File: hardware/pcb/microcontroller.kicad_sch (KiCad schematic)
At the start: 16 parts, among them U4 STM32G474CBT6TR, Y1 CS10820-24M

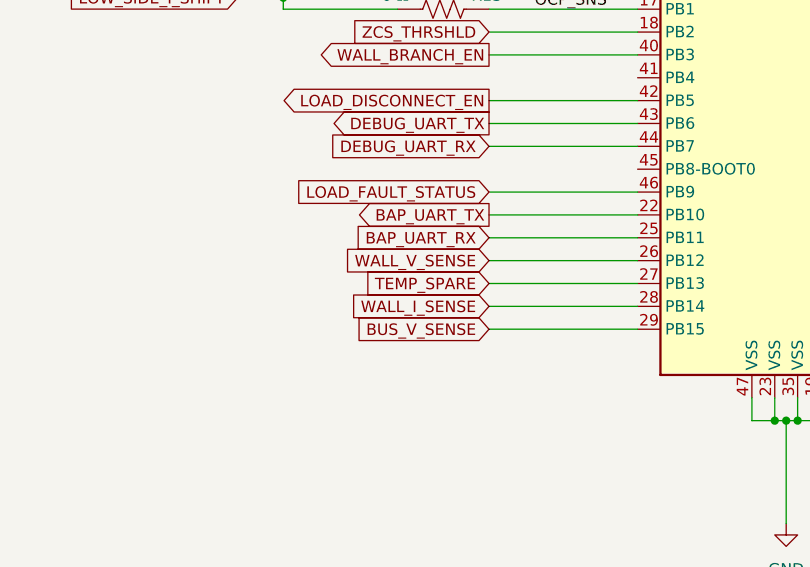
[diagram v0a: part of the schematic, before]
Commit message: Assign PB13 to delivered-load voltage sensing
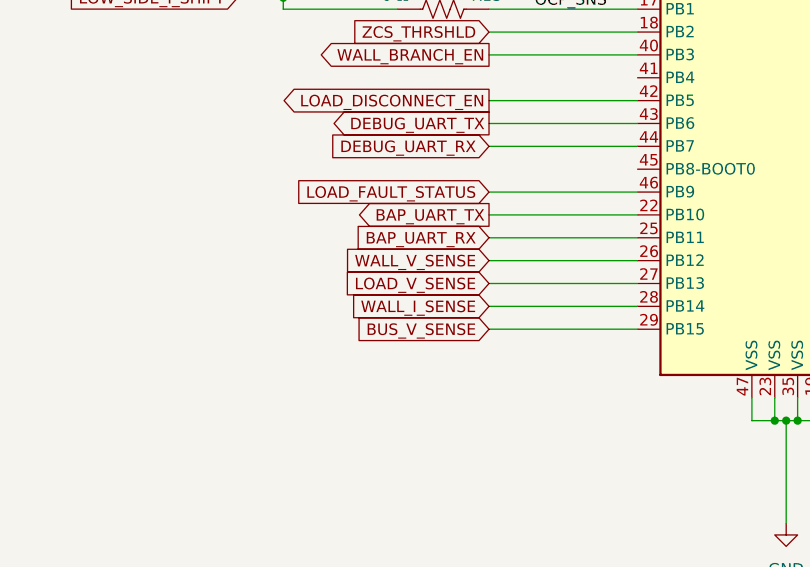
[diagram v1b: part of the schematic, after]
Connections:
- net TEMP_SPARE renamed LOAD_V_SENSE
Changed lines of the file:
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@@
 		)
 	)
-	(global_label "TEMP_SPARE"
+	(global_label "LOAD_V_SENSE"
 		(shape input)
 		(at 121.92 139.7 180)

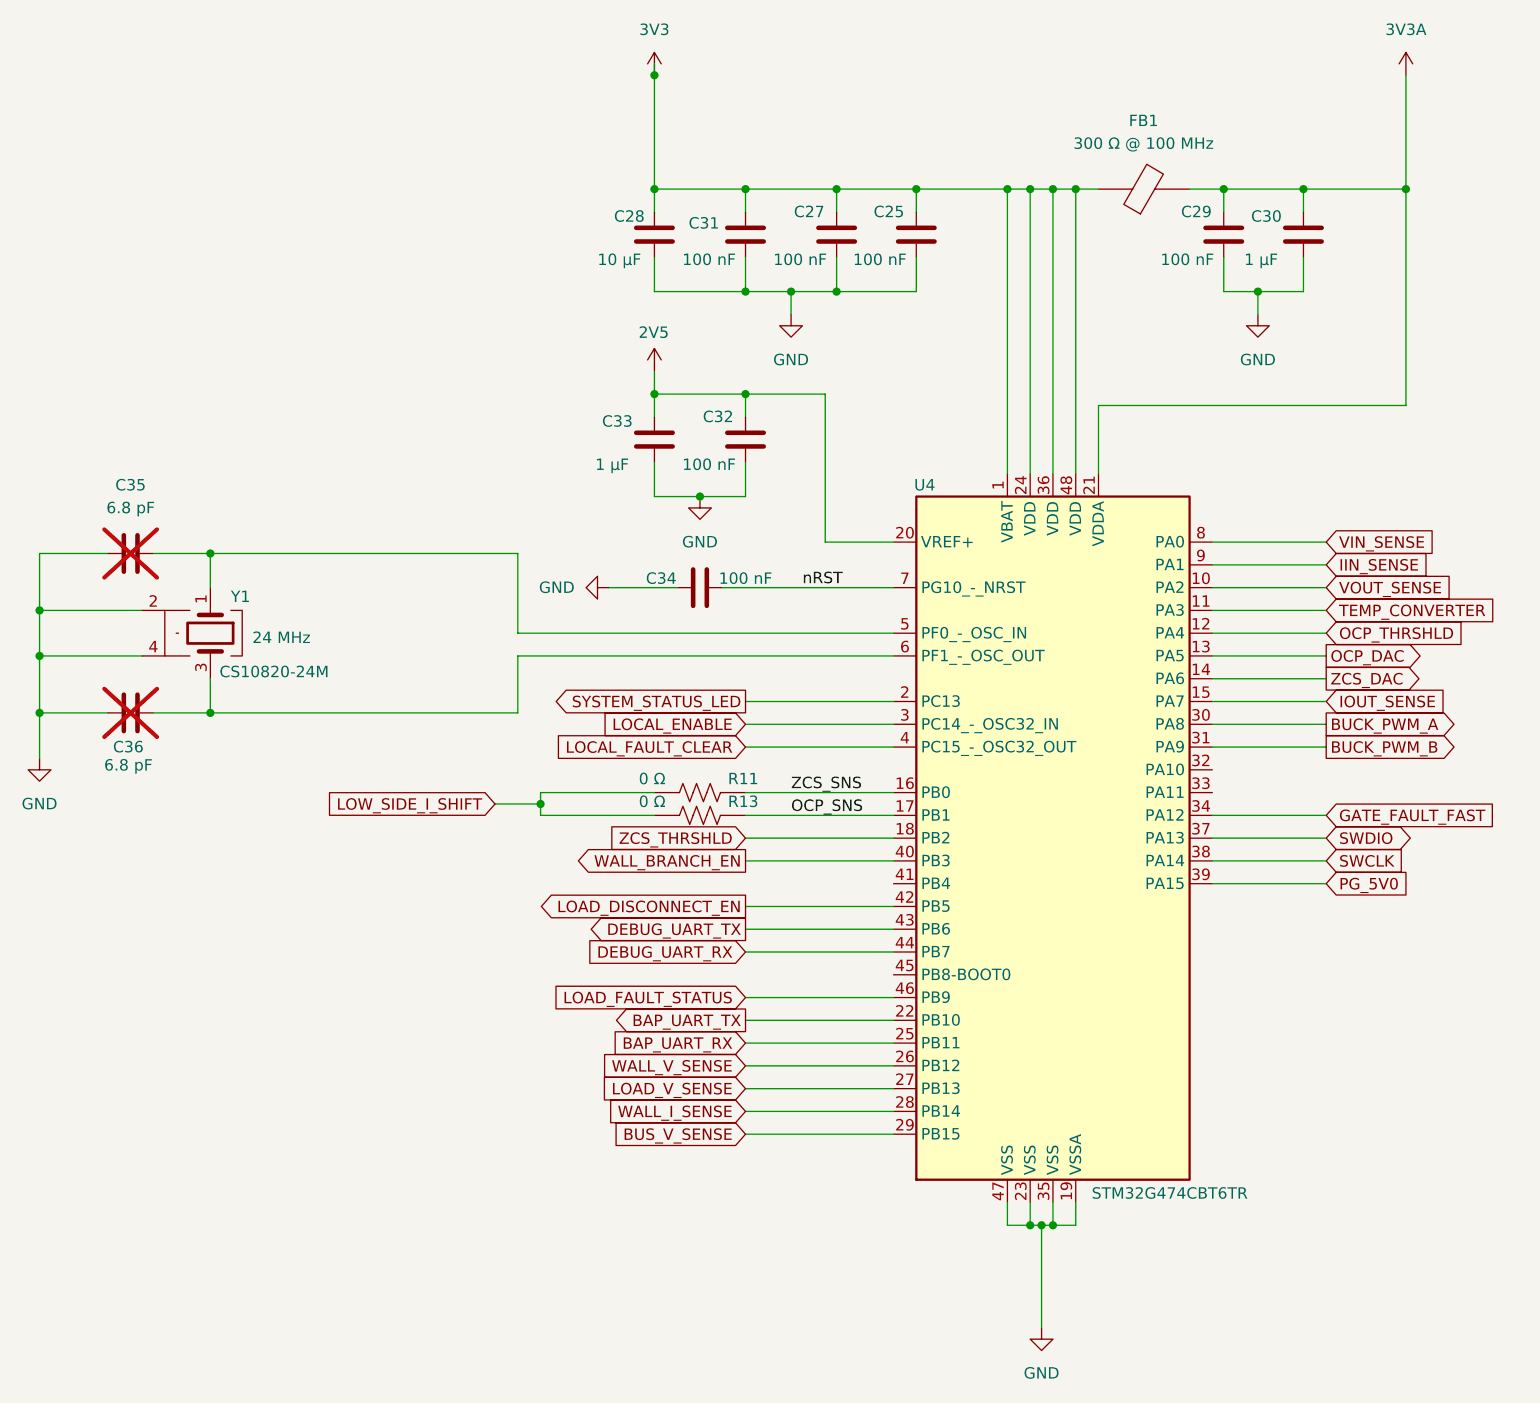
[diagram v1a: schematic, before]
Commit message: Replace legacy passive Specs with verified exact-MPN components
Migrate 51 instances across 20 identities and advance the public library pin to 8a4c96de. Preserve component references, UUIDs, placement, DNP flags, shared package geometry/models and exact pin-to-net connectivity. All ERC findings match baseline; PCB and unrelated components unchanged. Includes per-reference replacement report.
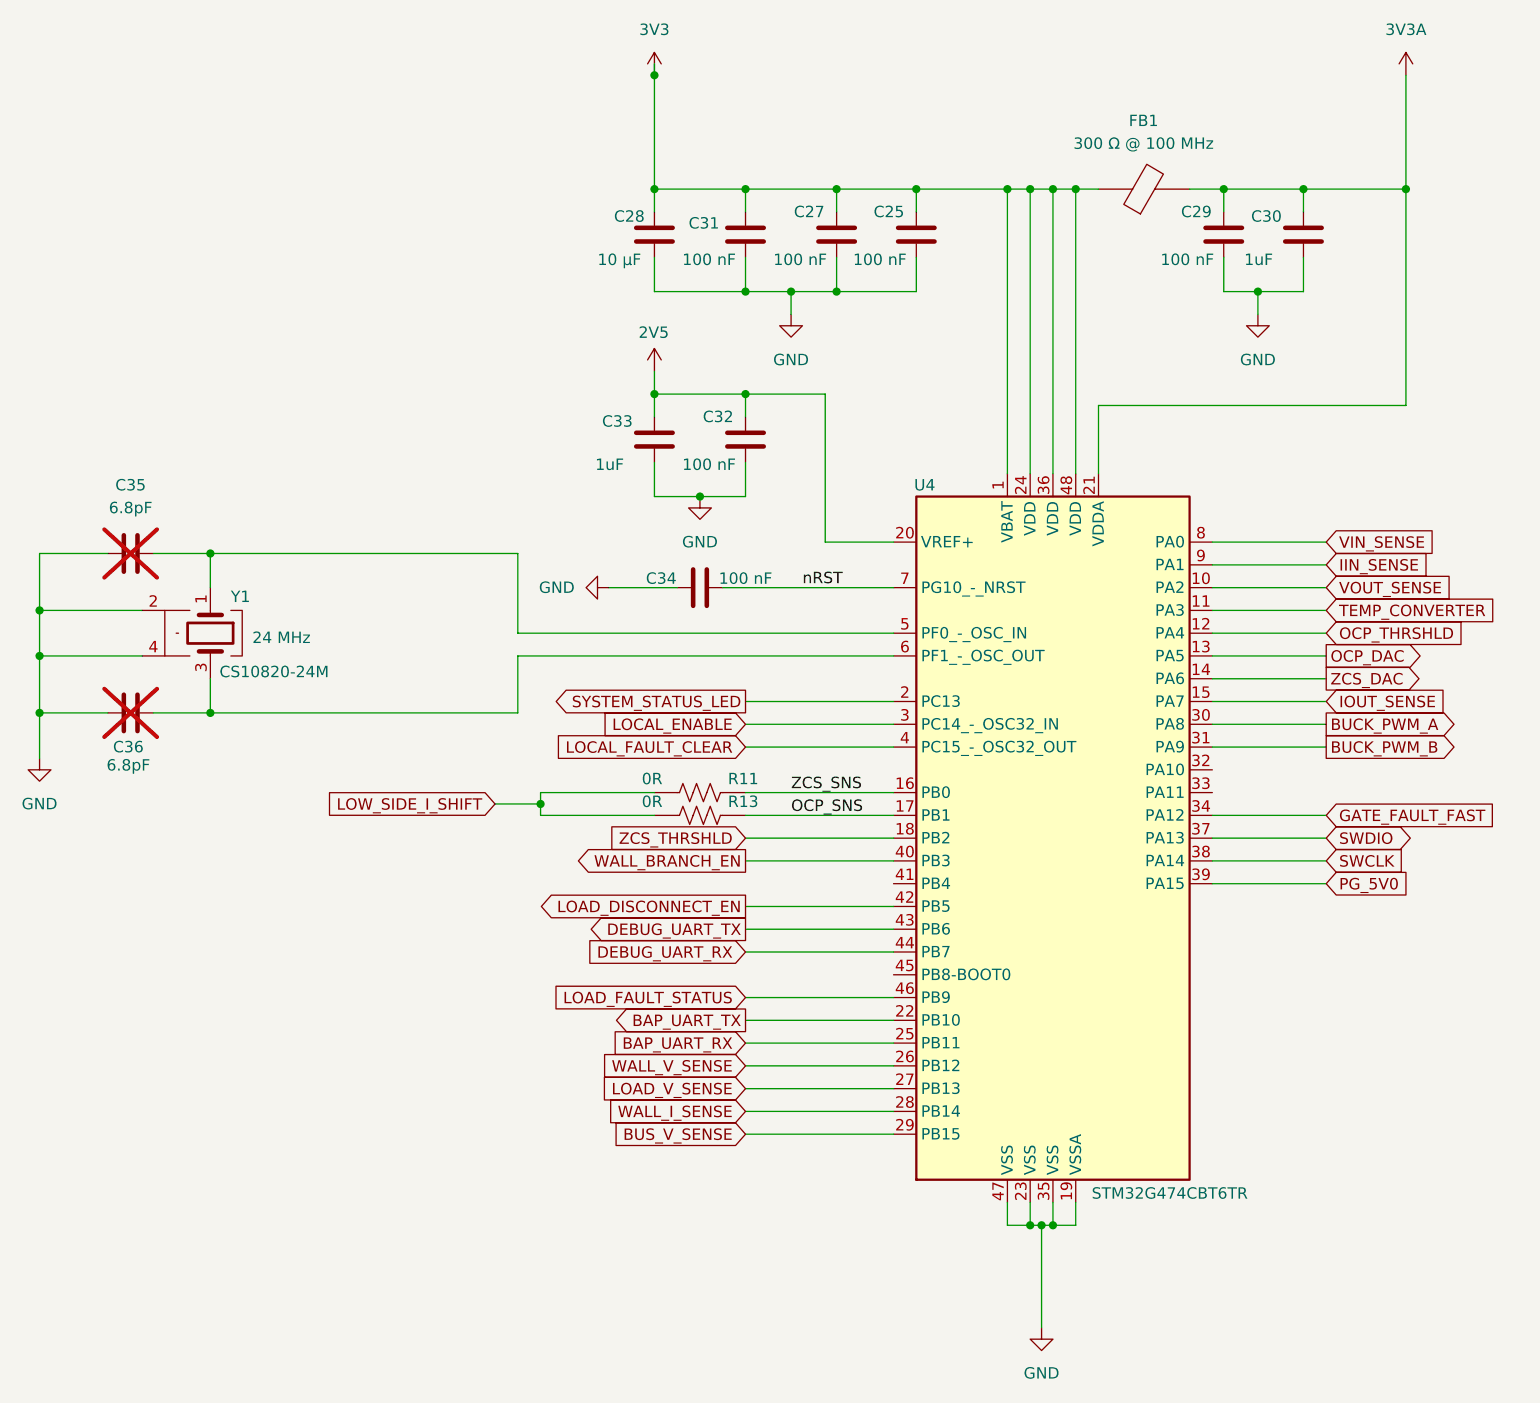
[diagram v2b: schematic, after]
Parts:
- C25, C27, C28, C29, C32, C34: symbol verified:P-00012 -> verified:GRM188R71E104KA01D; IPN P-00012 -> P-00061; IPN_Class Spec -> Part; Manufacturer 1 (none) -> Murata; Manufacturer Part Number 1 (none) -> GRM188R71E104KA01D; Operating Temperature (none) -> -55 to +125 deg C; Package 0603 (1608 Metric) -> 0603; Package Detail (none) -> 0603 (1608 Metric); Rating Conditions (none) -> Nominal 100 nF +/-10%, rated 25 Vdc; X7R temperature charac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; Rev_Creator golanaa -> Steve; Sym_Hash 2542b0e3e5ffcb98 -> c25b734526883d9e; Sym_Version 0.1.1 -> 0.1.0; Tolerance ±10% -> +/-10%; Type SMT -> SMD; Voltage Rating 25 V -> 25 Vdc
- C30, C33: value 1 µF -> 1uF; symbol verified:P-00021 -> verified:GRM21BR71E105KA99L; Capacitance Measurement (none) -> Room temperature; 1 kHz +/-10%; 1.0 +/-0.2 Vrms (spec p.2); DC Bias Limitation (none) -> Effective capacitance decreases with DC bias; exact bias cu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; IPN P-00021 -> P-00047; IPN_Class Spec -> Part; Legacy Comparison (none) -> Nominal 1uF,25V,X7R,+/-10%,0805 agree with legacy context; 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; Manufacturer 1 (none) -> Murata; Manufacturer Part Number 1 (none) -> GRM21BR71E105KA99L; Operating Temperature (none) -> -55 to +125 C; Package 0805 (2012 Metric) -> 0805; Package Detail (none) -> 0805 (2012 Metric); Part Origin (none) -> Exact-MPN symbol created by Steve. Reuses the unchanged rev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; Sym_Hash 1c28230c936da672 -> 0a95b6754c0f7212; Sym_Version 0.1.0 -> 0.1.1; Temperature Characteristic (none) -> +/-15% relative to 25 C over -55 to +125 C; no bias; Tolerance ±10% -> +/-10%; Voltage Rating 25 V -> 25 VDC
- C31: symbol verified:P-00028 -> verified:C2012X7R1A106K125AC; IPN P-00028 -> P-00026; IPN_Class Spec -> Part; Manufacturer 1 (none) -> TDK; Manufacturer Part Number 1 (none) -> C2012X7R1A106K125AC; Sym_Hash 1d2a882f45307465 -> 4d08d39523531888
- C35, C36: value 6.8 pF -> 6.8pF; symbol verified:P-00029 -> verified:04025A6R8JAT2A; Capacitance Measurement (none) -> 1 MHz ±10%, 1.0 Vrms ±0.2 V; C <=1000 pF; DC Bias (none) -> No exact-part quantitative bias curve established. Nominal 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; Dielectric C0G/NP0 -> C0G (NP0); IPN P-00029 -> P-00048; IPN_Class Spec -> Part; Manufacturer 1 (none) -> KYOCERA AVX; Manufacturer Part Number 1 (none) -> 04025A6R8JAT2A; Migration Notes (none) -> Nominal capacitance, voltage, dielectric, tolerance and siz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; Operating Temperature (none) -> -55 to +125 °C; Package 0402 (1005 Metric) -> 0402; Package Detail (none) -> 0402 (1005 Metric); Part Origin (none) -> Exact-MPN symbol created by Steve. Reuses the unchanged rev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; Q Minimum (none) -> 536 for 6.8 pF (400+20C, C<30 pF); same capacitance test co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; Sym_Hash 47f600e61f8d8c20 -> 3290f6115e6b1cb0; Sym_Version 0.1.0 -> 0.1.1; Temperature Coefficient (none) -> 0 ±30 ppm/°C, -55 to +125 °C; Type SMT -> Capacitor; Voltage Rating 50 V -> 50 VDC
- R11, R13: value 0 Ω -> 0R; symbol verified:P-00045 -> verified:RC0402JR-070RL; Derating (none) -> RC0402: ambient power curve 100% through 70 C, linearly to 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; IPN P-00045 -> P-00066; IPN_Class Spec -> Part; Manufacturer 1 (none) -> Yageo; Manufacturer Part Number 1 (none) -> RC0402JR-070RL; Maximum Current (none) -> 2 A; Maximum Current Detail (none) -> 2 A maximum; not the continuous rated current; Maximum Resistance 50 mΩ -> <50 mΩ; Maximum Working Voltage N/A (jumper; rated current governs) -> Not applicable as resistor voltage rating; zero-ohm jumper 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; Operating Temperature (none) -> -55 to +155 C; rated load derates above 70 C; Package 0402 (1005 Metric) -> 0402; Package Detail (none) -> 0402 (1005 metric); Part Origin (none) -> Manufacturer RC_L V14; reused reviewed managed R_0402_1005M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; Power Rating 62.5 mW -> 0.0625 W standard package rating at 70 C ambient; not termi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; Rated Current Detail (none) -> 1 A; apply ambient temperature derating above 70 C; Rating Conditions Rated current minimum at 70°C; derate above 70°C. Maximum r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 -> 70 °C ambient; derating above 70 °C; see thermal limits; Resistance Limit (none) -> <50 mOhm initial; Sym_Hash d8720a43ae1f727f -> 367b3db58b6621a4; Sym_Version 0.1.1 -> 0.1.0; Temperature Coefficient N/A (jumper) -> Not applicable (zero-ohm jumper); Tolerance N/A (jumper; maximum resistance governs) -> Not applicable (zero-ohm jumper; J is ordering code)
